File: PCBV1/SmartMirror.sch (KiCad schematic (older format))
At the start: 26 parts, among them J1 208658-1051, J2 502570-0893, J3 10118194-0001LF, J5 USB_A, J6 RJMG1BD3B8K1ANR, J7 10118194-0001LF, SW1 SW_DIP_x05, U14 TPD3E001DRLR, U15 TPD3E001DRLR, U3 CM1624-08DE, U4 TPD3E001DRLR

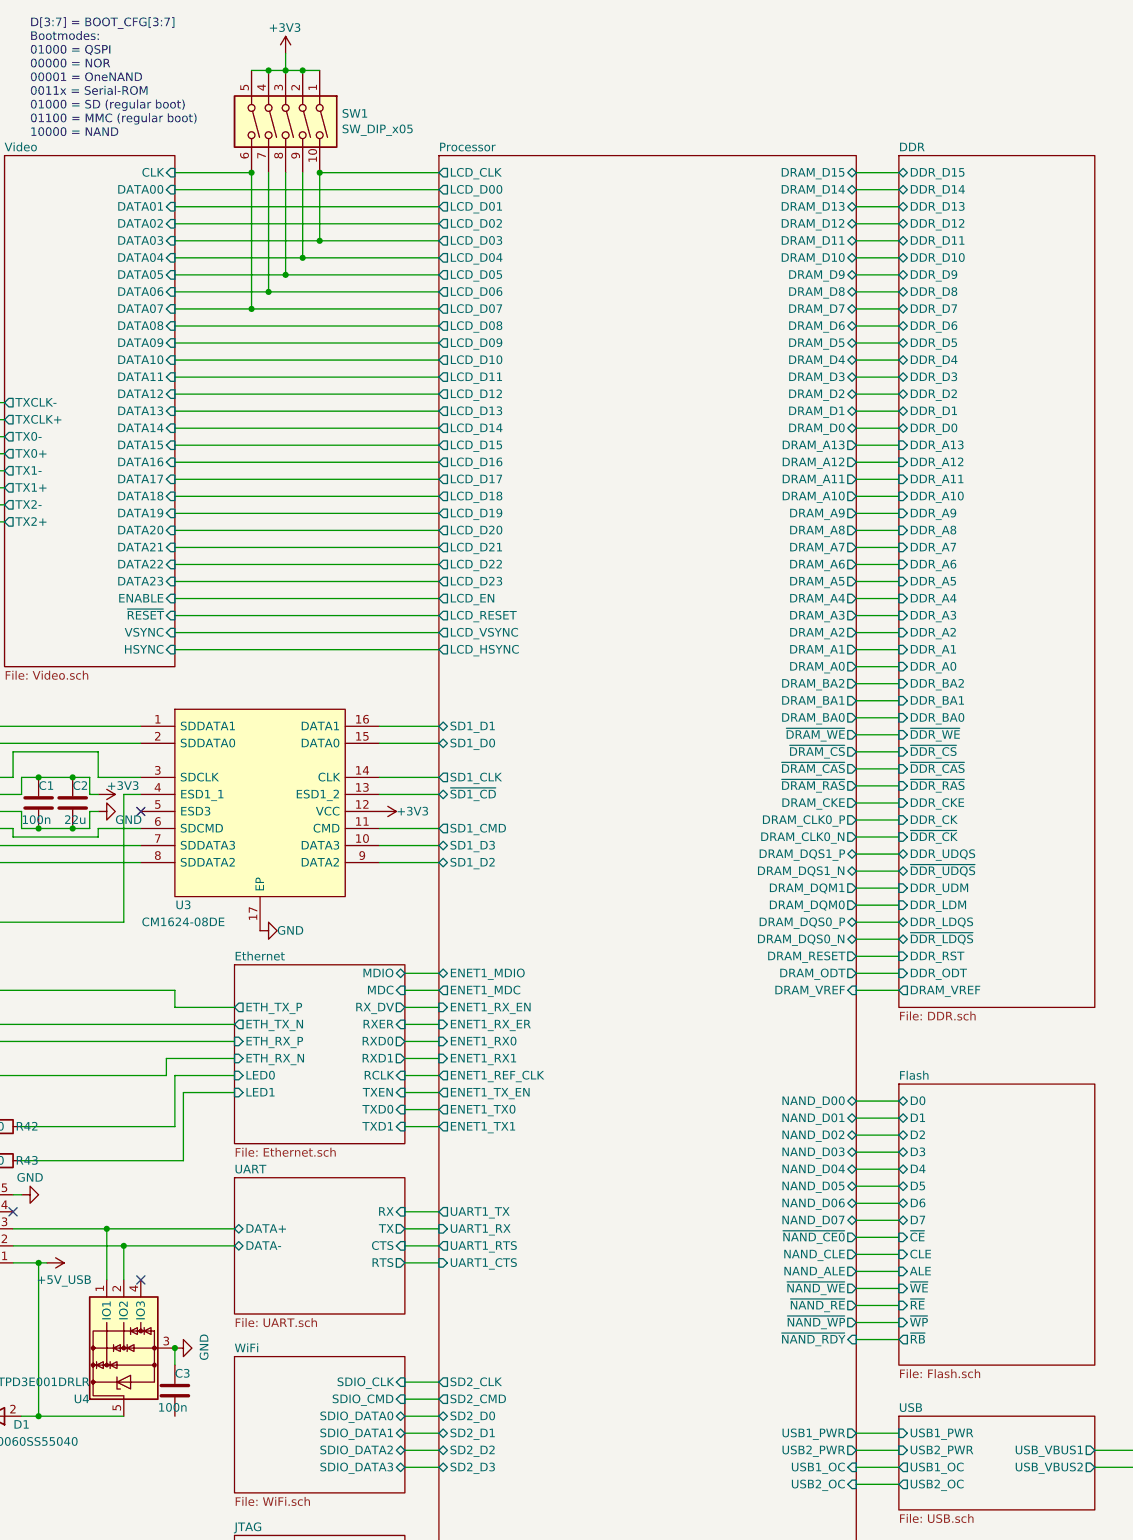
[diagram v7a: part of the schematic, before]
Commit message: Many changes to footprints (0603 -> 0402), basic DDR layout set, no traces made.
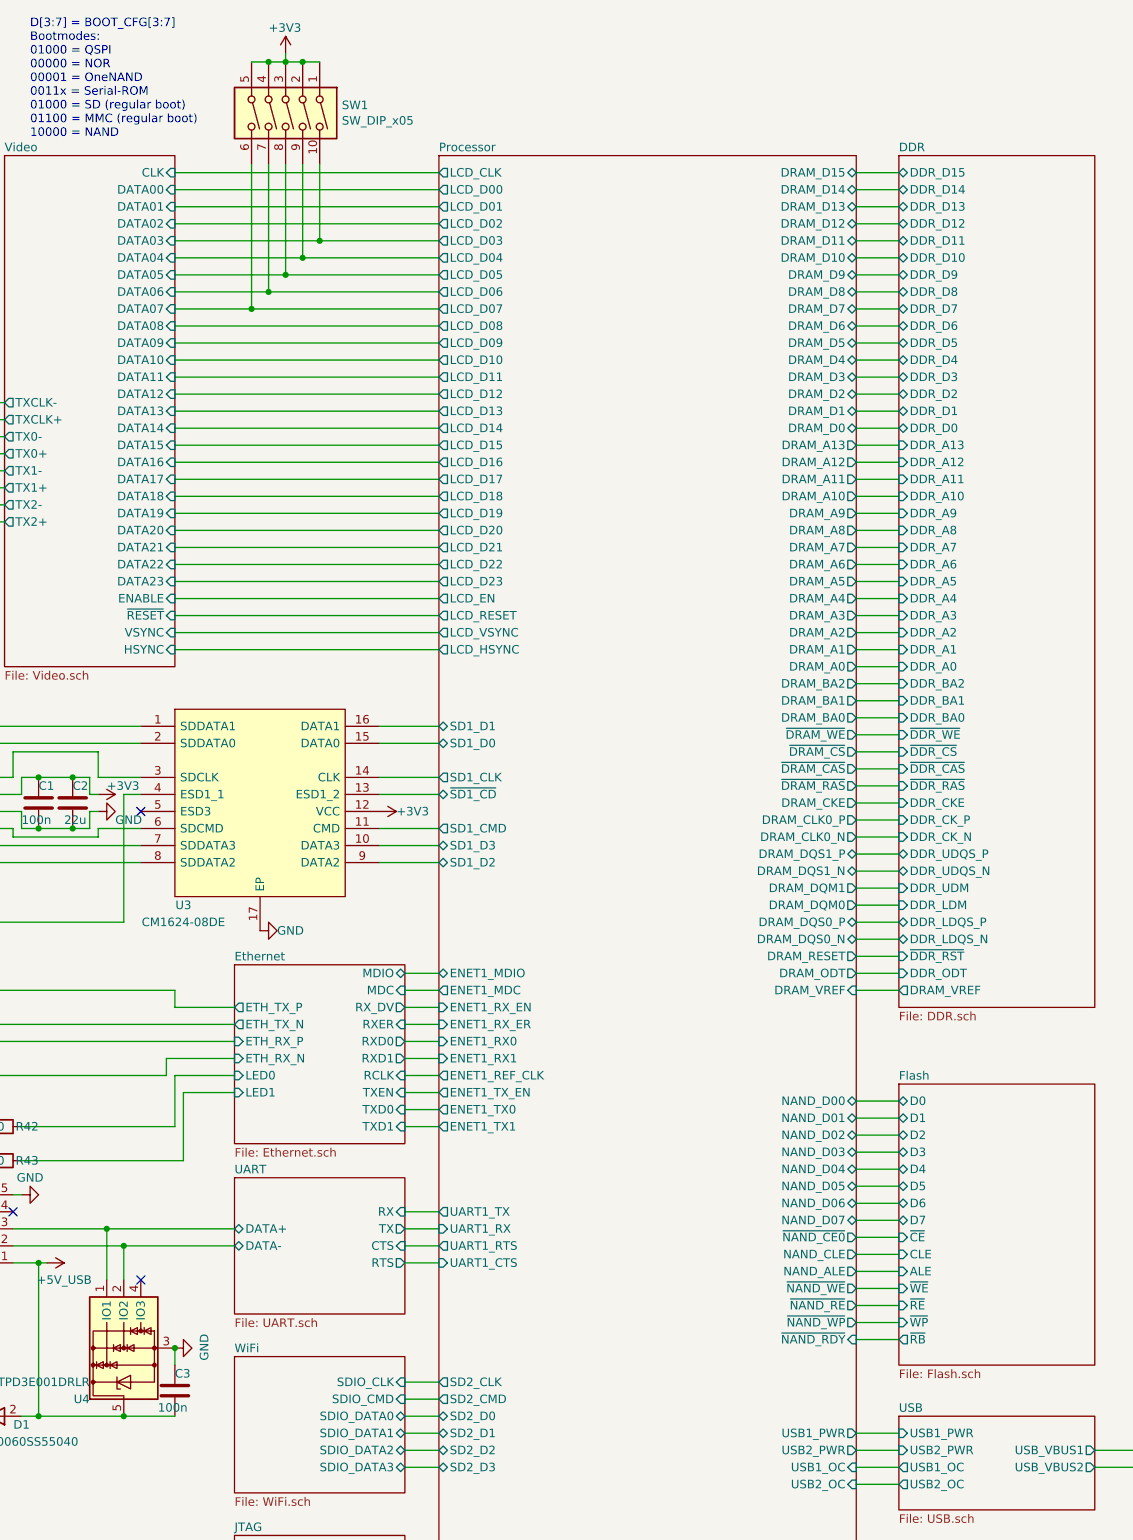
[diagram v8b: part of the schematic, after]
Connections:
- net +5V_USB: now also C3.2
- net Processor/LCD_CLK: no longer SW1.10
- new net Processor/LCD_D03: SW1.10
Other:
- moved on the sheet: SW1
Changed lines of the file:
@@
 F36 "~DDR_CS" I L 9700 5000 50
 F37 "DDR_CKE" I L 9700 5300 50
-F38 "~DDR_CK" I L 9700 5500 50
+F38 "DDR_CK_N" I L 9700 5500 50
 F39 "~DDR_CAS" I L 9700 5100 50
-F40 "DDR_CK" I L 9700 5400 50
+F40 "DDR_CK_P" I L 9700 5400 50
 F41 "~DDR_RAS" I L 9700 5200 50
-F42 "~DDR_UDQS" B L 9700 5700 50
-F43 "DDR_UDQS" B L 9700 5600 50
+F42 "DDR_UDQS_N" B L 9700 5700 50
+F43 "DDR_UDQS_P" B L 9700 5600 50
 F44 "DDR_UDM" I L 9700 5800 50
 F45 "DDR_LDM" I L 9700 5900 50
-F46 "DDR_LDQS" B L 9700 6000 50
-F47 "~DDR_LDQS" B L 9700 6100 50
-F48 "DDR_RST" I L 9700 6200 50
+F46 "DDR_LDQS_P" B L 9700 6000 50
+F47 "DDR_LDQS_N" B L 9700 6100 50
+F48 "~DDR_RST" I L 9700 6200 50
 F49 "DDR_ODT" I L 9700 6300 50
 F50 "DRAM_VREF" O L 9700 6400 50
@@
 Wire Wire Line
 	5450 2400 5900 2400
-Wire Wire Line
-	6200 1600 6200 2100
 Connection ~ 6200 2100
 Wire Wire Line
 	6200 2100 7000 2100
-Wire Wire Line
-	6100 1600 6100 2200
 Connection ~ 6100 2200
 Wire Wire Line
 	6100 2200 7000 2200
-Wire Wire Line
-	6000 1600 6000 2300
 Connection ~ 6000 2300
 Wire Wire Line
 	6000 2300 7000 2300
-Wire Wire Line
-	5900 1600 5900 2400
 Connection ~ 5900 2400
 Wire Wire Line
@@
 	7000 9200 6800 9200
 Wire Wire Line
-	5900 1000 6000 1000
-$Comp
-L Switch:SW_DIP_x05 SW1
-U 1 1 62A00778
-P 6100 1300
-F 0 "SW1" V 6054 1630 50  0000 L CNN
-F 1 "SW_DIP_x05" V 6145 1630 50  0000 L CNN
-F 2 "Button_Switch_SMD:SW_DIP_SPSTx05_Slide_6.7x14.26mm_W6.73mm_P2.54mm_LowProfile_JPin" H 6100 1300 50  0001 C CNN
-F 3 "https://www.mouser.dk/datasheet/2/96/219-1144706.pdf" H 6100 1300 50  0001 C CNN
-F 4 "219-5MST" V 6100 1300 50  0001 C CNN "Name"
-	1    6100 1300
-	0    1    1    0
-$EndComp
-Wire Wire Line
-	6000 1000 6100 1000
-Connection ~ 6000 1000
-Connection ~ 6100 1000
-Wire Wire Line
-	6100 1000 6200 1000
-Connection ~ 6200 1000
-Wire Wire Line
-	6200 1000 6300 1000
-Wire Wire Line
-	6100 1000 6100 900
-Wire Wire Line
 	5450 2000 6300 2000
-Wire Wire Line
-	6300 1600 6300 2000
 Connection ~ 6300 2000
 Wire Wire Line
@@
 Text Notes 4600 1400 0    50   ~ 0
 D[3:7] = BOOT_CFG[3:7]\nBootmodes:\n01000 = QSPI\n00000 = NOR\n00001 = OneNAND\n0011x = Serial-ROM\n01000 = SD (regular boot)\n01100 = MMC (regular boot)\n10000 = NAND
-Wire Wire Line
-	5450 1600 5900 1600
 Wire Wire Line
 	5450 1700 7000 1700
@@
 	12500 7050 12750 7050
 Wire Wire Line
-	6300 1600 7000 1600
-Connection ~ 5900 1600
-Connection ~ 6300 1600
-Wire Wire Line
 	4500 7900 5150 7900
 Wire Wire Line
@@
 Wire Wire Line
 	5500 7400 4550 7400
+Wire Wire Line
+	5150 8900 5450 8900
+Connection ~ 5150 8900
+Wire Wire Line
+	6200 1550 6200 2100
+Wire Wire Line
+	6100 1550 6100 2200
+Wire Wire Line
+	6000 1550 6000 2300
+Wire Wire Line
+	5900 1550 5900 2400
+Connection ~ 6000 950
+Wire Wire Line
+	5900 950  6000 950
+Wire Wire Line
+	6100 950  6100 900
+Connection ~ 6100 950
+Wire Wire Line
+	6000 950  6100 950
+Connection ~ 6200 950
+Wire Wire Line
+	6100 950  6200 950
+Wire Wire Line
+	6300 1550 6300 2000
+Wire Wire Line
+	6200 950  6300 950
+$Comp
+L Switch:SW_DIP_x05 SW1
+U 1 1 62A00778
+P 6100 1250
+F 0 "SW1" V 6054 1580 50  0000 L CNN
+F 1 "SW_DIP_x05" V 6145 1580 50  0000 L CNN
+F 2 "Button_Switch_SMD:SW_DIP_SPSTx05_Slide_6.7x14.26mm_W6.73mm_P2.54mm_LowProfile_JPin" H 6100 1250 50  0001 C CNN
+F 3 "https://www.mouser.dk/datasheet/2/96/219-1144706.pdf" H 6100 1250 50  0001 C CNN
+F 4 "219-5MST" V 6100 1250 50  0001 C CNN "Name"
+	1    6100 1250
+	0    1    1    0
+$EndComp
+Wire Wire Line
+	5450 1600 7000 1600
 $EndSCHEMATC
